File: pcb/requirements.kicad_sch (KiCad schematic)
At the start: 10 parts

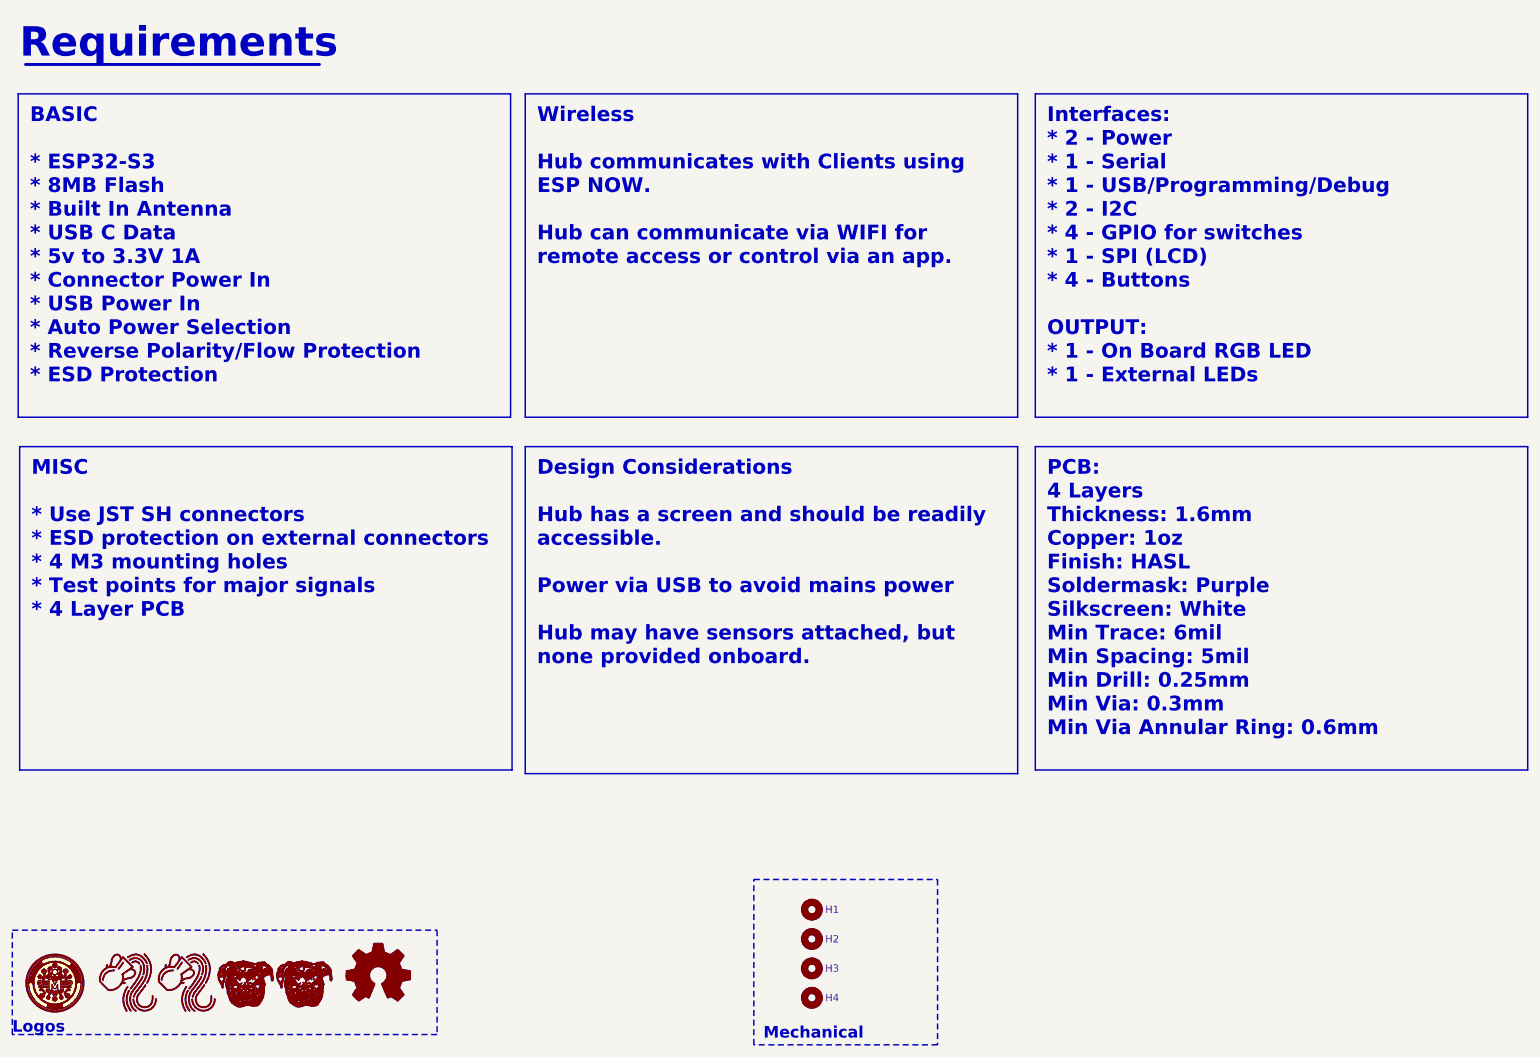
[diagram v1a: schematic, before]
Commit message: Fixed power input
Removed 3.3v selection
Removed unnecessary caps
Rerouted as necessary
Fixed silkscreen
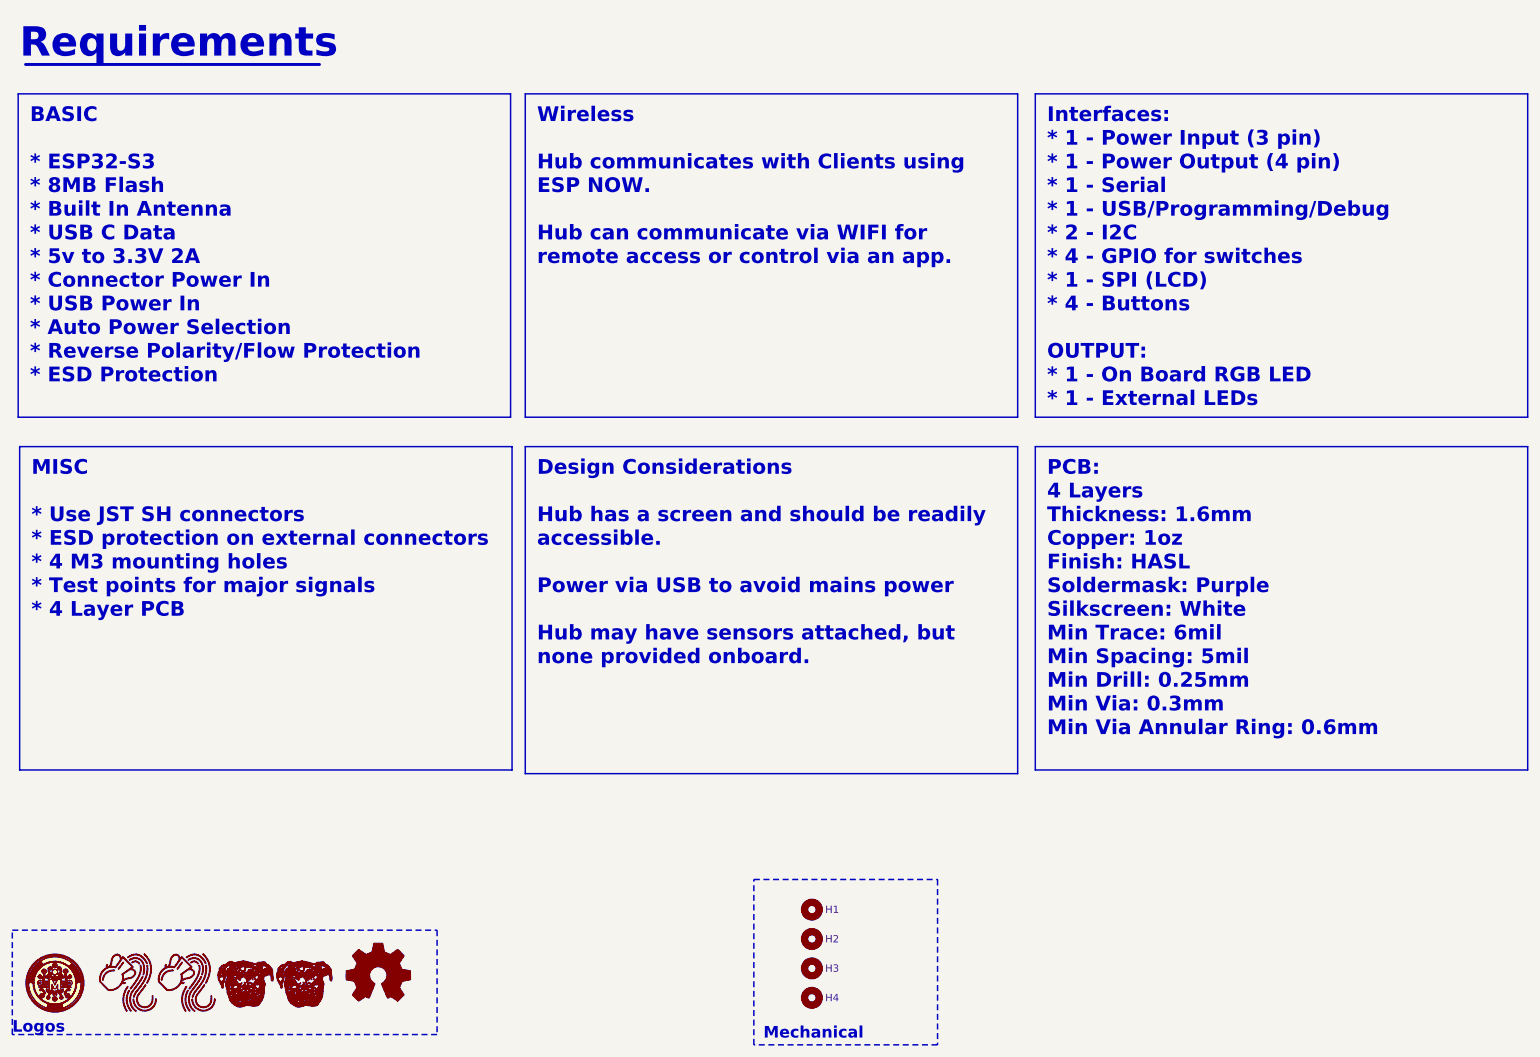
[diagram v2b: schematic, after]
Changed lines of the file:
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@@
 		)
 	)
-	(text_box "BASIC\n\n* ESP32-S3\n* 8MB Flash\n* Built In Antenna\n* USB C Data\n* 5v to 3.3V 1A\n* Connector Power In\n* USB Power In\n* Auto Power Selection\n* Reverse Polarity/Flow Protection\n* ESD Protection"
+	(text_box "BASIC\n\n* ESP32-S3\n* 8MB Flash\n* Built In Antenna\n* USB C Data\n* 5v to 3.3V 2A\n* Connector Power In\n* USB Power In\n* Auto Power Selection\n* Reverse Polarity/Flow Protection\n* ESD Protection"
 		(exclude_from_sim yes)
 		(at 16.51 30.48 0)
@@
 		)
 	)
-	(text_box "Interfaces:\n* 2 - Power\n* 1 - Serial\n* 1 - USB/Programming/Debug\n* 2 - I2C\n* 4 - GPIO for switches\n* 1 - SPI (LCD)\n* 4 - Buttons\n\nOUTPUT:\n* 1 - On Board RGB LED\n* 1 - External LEDs"
+	(text_box "Interfaces:\n* 1 - Power Input (3 pin)\n* 1 - Power Output (4 pin)\n* 1 - Serial\n* 1 - USB/Programming/Debug\n* 2 - I2C\n* 4 - GPIO for switches\n* 1 - SPI (LCD)\n* 4 - Buttons\n\nOUTPUT:\n* 1 - On Board RGB LED\n* 1 - External LEDs"
 		(exclude_from_sim yes)
 		(at 192.278 30.48 0)

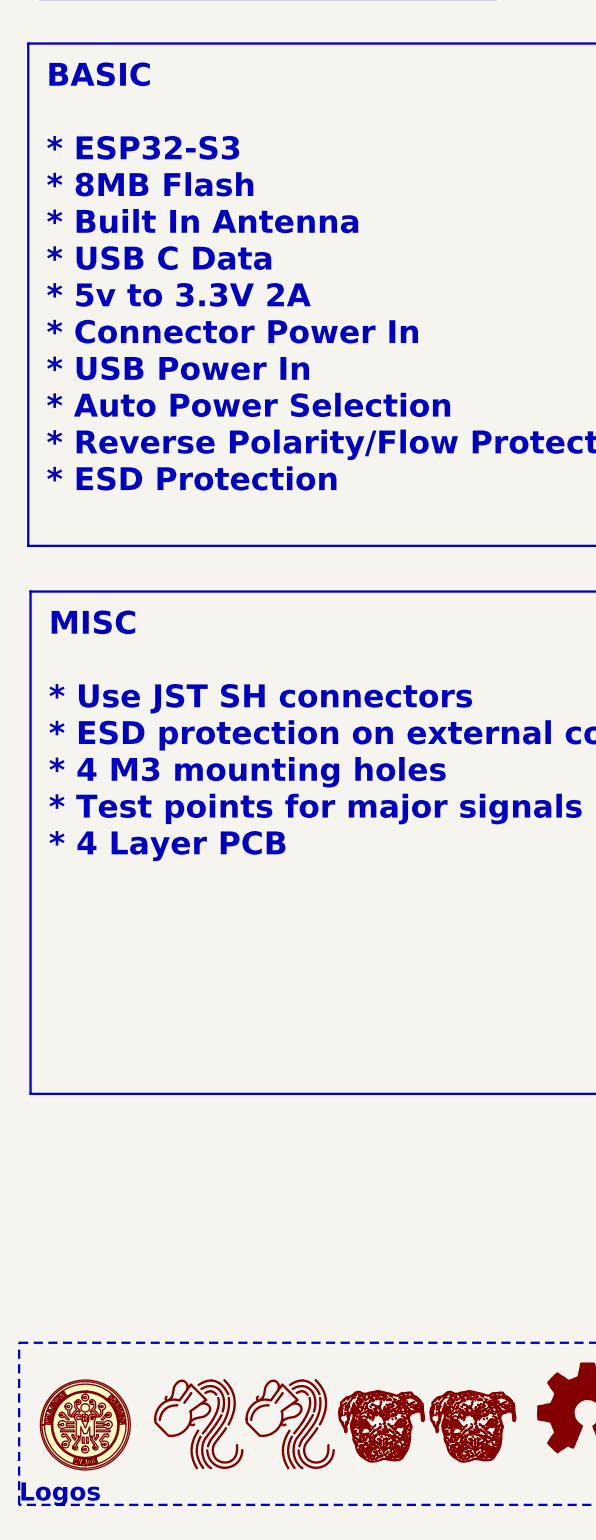
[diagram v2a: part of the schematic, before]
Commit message: Minor silkscreen changes.
Updated 2222 footprint
Ready for next release
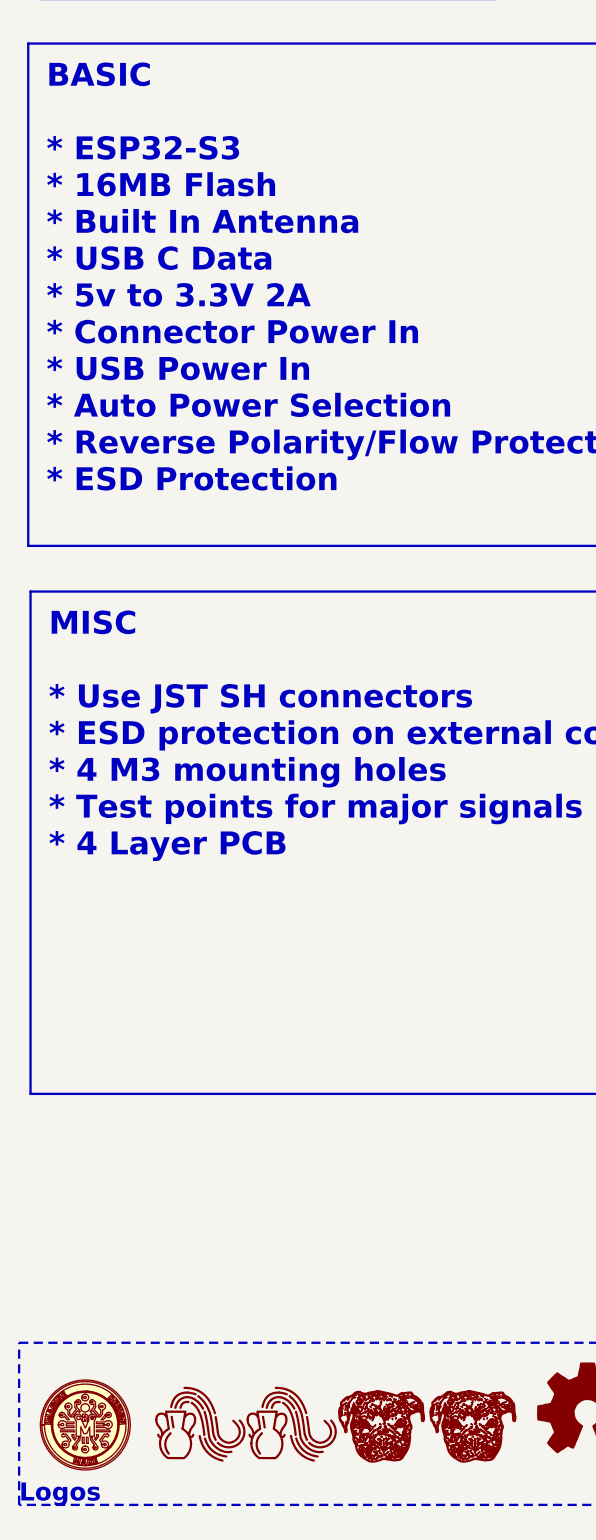
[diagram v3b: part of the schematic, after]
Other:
- title: Aquarius Hub -> Aquarius Node
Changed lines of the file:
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@@
 	(paper "A4")
 	(title_block
-		(title "Aquarius Hub")
+		(title "Aquarius Node")
 		(date "<<release-date>>")
 		(rev "<<tag>>")
@@
 		)
 	)
-	(text_box "BASIC\n\n* ESP32-S3\n* 8MB Flash\n* Built In Antenna\n* USB C Data\n* 5v to 3.3V 2A\n* Connector Power In\n* USB Power In\n* Auto Power Selection\n* Reverse Polarity/Flow Protection\n* ESD Protection"
+	(text_box "BASIC\n\n* ESP32-S3\n* 16MB Flash\n* Built In Antenna\n* USB C Data\n* 5v to 3.3V 2A\n* Connector Power In\n* USB Power In\n* Auto Power Selection\n* Reverse Polarity/Flow Protection\n* ESD Protection"
 		(exclude_from_sim yes)
 		(at 16.51 30.48 0)

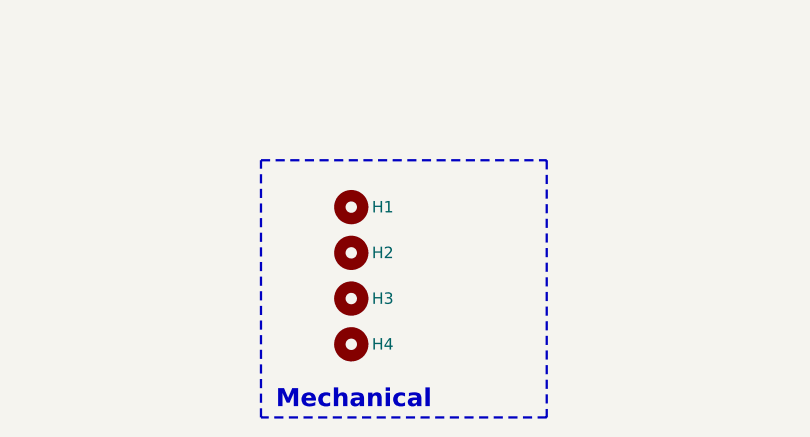
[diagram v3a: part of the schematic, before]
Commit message: Temoved duplicative test points
Cleaned up routing and silkscreen.
Updated mounting holes and tied to ground.
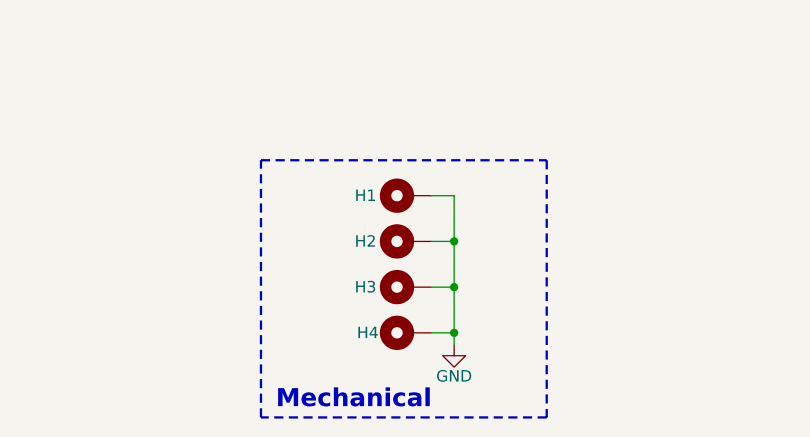
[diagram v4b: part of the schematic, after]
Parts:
- H1, H2, H3, H4: symbol Mechanical:MountingHole -> CRGM Mechanical:MountingHole_Pad
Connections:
- new net GND: H1.1, H2.1, H3.1, H4.1

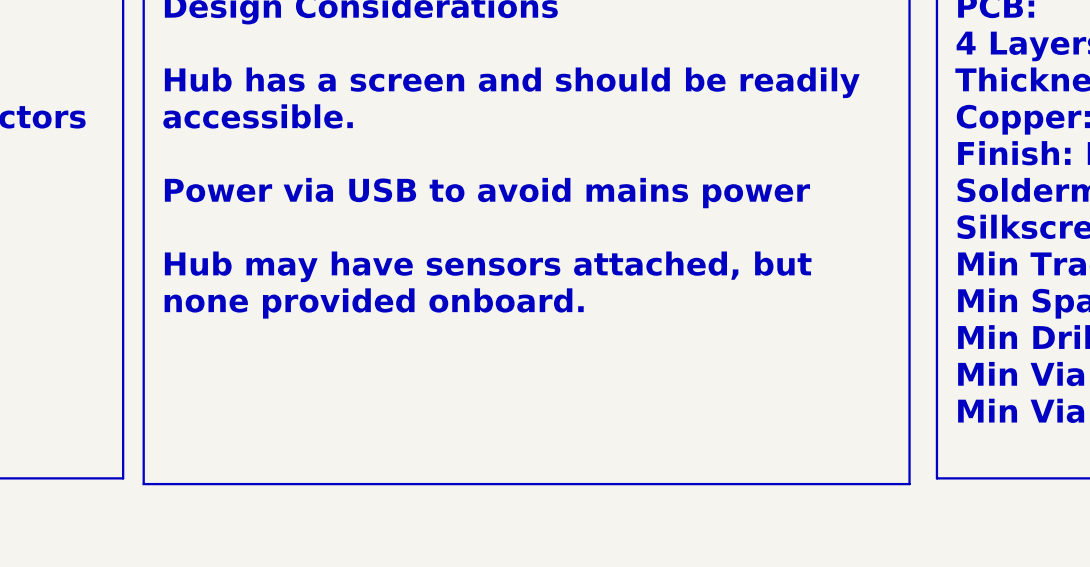
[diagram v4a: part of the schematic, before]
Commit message: Fixed part placement and missing model
Both display and 3.3 regulator were in the wrong place after updating from library!
LED was missing model
Minor silkscreen changes
Updated renders
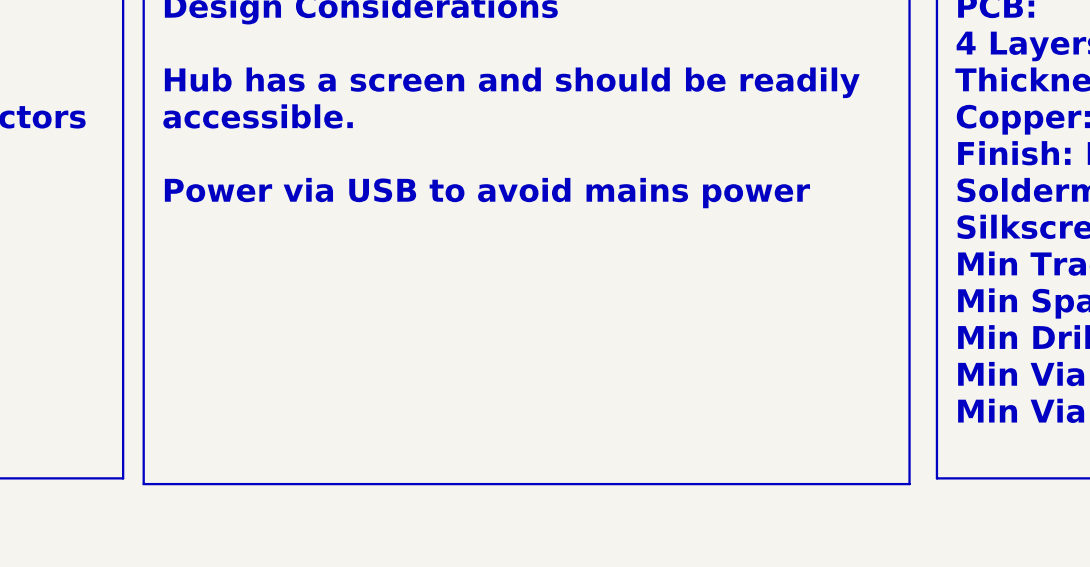
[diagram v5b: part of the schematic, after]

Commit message: Added analog port
re-routed
resized the pretty princess
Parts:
- LOGO5: footprint CRGM Logos:Roxy 8mm -> CRGM Logos:Roxy 6.5mm
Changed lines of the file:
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@@
 			)
 		)
-		(property "Footprint" "CRGM Logos:Roxy 8mm"
+		(property "Footprint" "CRGM Logos:Roxy 6.5mm"
 			(at 55.88 192.278 0)
 			(effects
